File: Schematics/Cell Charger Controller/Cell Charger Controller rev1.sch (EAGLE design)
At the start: 17 parts, among them U1 HM2102NLT

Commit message: board almost done
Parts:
- added 12V_IN, CURRENT_IN, CURRENT_OUT: CONNECTOR-2, HyTechDevices:CONNECTOR-2
- added C2: 0.1uF, HyTechDevices:CAP0603-CAP
- added C3: 1uF, HyTechDevices:CAP0603-CAP
- added C6, C7: 10uF, HyTechDevices:CAP0603-CAP
- added D103: TS4148 RYG, HyTechDevices:DIODE0805
- added D104: MMBZ5246BLT1G, HyTechDevices:DIODE_ZENER
- added F1: 10A, HyTechDevices:FUSE_MINIBLADE
- added ISO-SPI, THERM1, THERM2, THERM3, THERM4, THERM5, THERM6, THERM7, THERM8, THERM9: CONNECTOR-2NANO-FIT_VERTICAL-2, HyTechDevices:CONNECTOR-2NANO-FIT_VERTICAL-2
- added Q1: DMG3406L, HyTechDevices:DMG3406LSOT
- added R14, R15, R16, R17, R18, R19, R20, R21, R22, R23: 10k, HyTechDevices:RESISTOR0603
- added U$10: OKI-78SR-5, HyTechDevices:OKI-78SR-5
- added U$4: INA260, HyTechDevices:INA260
- added U$5: MCP2562FD, HyTechDevices:MCP2562FD
- added U$6: ADAFRUIT_1824_KEYPAD, HyTechDevices:ADAFRUIT_1824_KEYPAD
- added U$7: ILI9341_TOUCH_SCREEN, HyTechDevices:ILI9341_TOUCH_SCREEN
- added U$8: G5LE-1A4, HyTechDevices:G5LE-1A4
- R10, R13, R9: value (none) -> 0
- R11, R12, R6, R7: value (none) -> 10k
- R8: value (none) -> 100
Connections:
- new net +12V: 12V_IN.1, C6.1, U$10.IN
- new net ALERT_INA: U$4.ALERT
- new net C1_KEYPAD: U$2.D35, U$6.C1
- new net C2_KEYPAD: U$2.D34, U$6.C2
- new net C3_KEYPAD: U$2.D33, U$6.C3
- new net CANH: U$5.7
- new net CANL: U$5.6
- new net CAN_RX: U$2.D0(RX1), U$5.4
- new net CAN_TX: U$2.D1(TX1), U$5.1
- new net CS_DISPLAY: U$2.D10, U$7.CS
- new net CS_DISPLAY_T: U$2.D9, U$7.T_CS
- new net CURRENT_IN: F1.2, U$8.P
- new net CURRENT_OUT: CURRENT_OUT.1, CURRENT_OUT.2, U$4.IN-
- new net D/C_DISPLAY: U$2.A1(RX3), U$7.DC
- new net IRQ_DISPLAY: U$2.D7(RX2), U$7.T_IRQ
- new net N$10: R8.1, U$7.LED
- new net N$11: CURRENT_IN.1, CURRENT_IN.2, F1.1
- new net N$12: R9.1, U$4.IN+, U$8.S
- new net N$15: D103.A, Q1.D, U$8.COIL+
- new net N$6: R11.2, R13.2, U$4.A1
- new net N$7: R10.1, R12.2, U$4.A0
- new net N$8: U$5.8
- new net N$9: R9.2, U$4.VBUS
- new net R1_KEYPAD: U$2.D32, U$6.R1
- new net R2_KEYPAD: U$2.D31(CANTX3), U$6.R2
- new net R3_KEYPAD: U$2.D30(CANRX3), U$6.R3
- new net R4_KEYPAD: U$2.D29, U$6.R4
- new net RELAY_CTRL: D104.C, Q1.G, R23.2, U$2.D5
- new net SCL_TEENSY: R7.2, U$2.A5, U$4.SCL
- new net SDA_TEENSY: R6.2, U$2.A4, U$4.SDA
- new net SENSE_THERM1: R14.1, THERM1.1, U$2.A14
- new net SENSE_THERM2: R15.1, THERM2.1, U$2.A15
- new net SENSE_THERM3: R16.1, THERM3.1, U$2.A16
- new net SENSE_THERM4: R17.1, THERM4.1, U$2.A17
- new net SENSE_THERM5: R18.1, THERM5.1, U$2.A2
- new net SENSE_THERM6: R19.1, THERM6.1, U$2.A10
- new net SENSE_THERM7: R20.1, THERM7.1, U$2.A11
- new net SENSE_THERM8: R21.1, THERM8.1, U$2.A12
- new net SENSE_THERM9: R22.1, THERM9.1, U$2.A13
- net +3V3: now also R8.2, U$2.3.3V, U$5.5, U$7.RESET
- net +5V: now also C2.1, C3.1, C7.1, D103.C, R10.2, R13.1, R14.2, R15.2, R16.2, R17.2, R18.2, R19.2, R20.2, R21.2, R22.2, R6.1, R7.1, U$10.OUT, U$4.VS, U$5.3, U$7.VCC, U$8.COIL-
- net CS_LTC6820: now also U$2.D6; no longer U$2.D10
- net GND: now also 12V_IN.2, C2.2, C3.2, C6.2, C7.2, D104.A, Q1.S, R11.1, R12.1, R23.1, THERM1.2, THERM2.2, THERM3.2, THERM4.2, THERM5.2, THERM6.2, THERM7.2, THERM8.2, THERM9.2, U$10.GND, U$2.GND, U$2.GND3, U$4.GND, U$5.2, U$7.GND
- net ISOSPI-N: now also ISO-SPI.2
- net ISOSPI-P: now also ISO-SPI.1
- net MISO_TEENSY: now also U$7.MISO, U$7.T_DO
- net MOSI_TEENSY: now also U$7.MOSI, U$7.T_DIN
- net SCK_TEENSY: now also U$7.SCK, U$7.T_CLK
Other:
- note added: "INA260"
- note added: "LTC6820"
- note added: "MCP2562"
- note added: "NOTE: Relay Coil Voltage - 5VDC"
- note added: "NOTE: The name of pins 5 and 8 on ths MCP2562 symbol are not correct, but the circuit should still work."
- moved on the sheet: C1, R1, R10, R11, R12, R13, R2, R3, R4, R5, R6, R7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

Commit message: charger controller board ready for review
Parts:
- added X1: CONNECTOR-4NANO-FIT-VERTICAL-4, HyTechDevices:CONNECTOR-4NANO-FIT-VERTICAL-4
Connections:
- net +12V: now also X1-1.S
- net ALERT_INA: now also U$2.A3
- net CANH: now also X1-4.S
- net CANL: now also X1-3.S
- net GND: now also X1-2.S
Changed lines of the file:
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@@
 <part name="D103" library="HyTechDevices" deviceset="DIODE" device="0805" value="TS4148 RYG"/>
 <part name="GND21" library="HyTechSupplies" deviceset="GND" device=""/>
+<part name="X1" library="HyTechDevices" deviceset="CONNECTOR-4" device="NANO-FIT-VERTICAL-4"/>
+<part name="GND22" library="HyTechSupplies" deviceset="GND" device=""/>
+<part name="P+14" library="HyTechSupplies" deviceset="+12V" device=""/>
 </parts>
 <sheets>
@@
 <attribute name="VALUE" x="215.9" y="208.28" size="1.778" layer="96"/>
 </instance>
+<instance part="X1" gate="-1" x="289.56" y="116.84" smashed="yes" rot="MR0">
+<attribute name="NAME" x="287.02" y="116.078" size="1.524" layer="95" rot="MR0"/>
+<attribute name="VALUE" x="295.402" y="120.777" size="1.778" layer="96" rot="MR0"/>
+</instance>
+<instance part="X1" gate="-2" x="289.56" y="114.3" smashed="yes" rot="MR0">
+<attribute name="NAME" x="287.02" y="113.538" size="1.524" layer="95" rot="MR0"/>
+</instance>
+<instance part="X1" gate="-3" x="289.56" y="111.76" smashed="yes" rot="MR0">
+<attribute name="NAME" x="287.02" y="110.998" size="1.524" layer="95" rot="MR0"/>
+</instance>
+<instance part="X1" gate="-4" x="289.56" y="109.22" smashed="yes" rot="MR0">
+<attribute name="NAME" x="287.02" y="108.458" size="1.524" layer="95" rot="MR0"/>
+</instance>
+<instance part="GND22" gate="1" x="302.26" y="111.76" smashed="yes" rot="MR0">
+<attribute name="VALUE" x="304.8" y="109.22" size="1.778" layer="96" rot="MR0"/>
+</instance>
+<instance part="P+14" gate="1" x="302.26" y="121.92" smashed="yes">
+<attribute name="VALUE" x="304.8" y="127" size="1.778" layer="96" rot="R180"/>
+</instance>
 </instances>
 <busses>
@@
 <pinref part="GND21" gate="1" pin="GND"/>
 <wire x1="218.44" y1="213.36" x2="218.44" y2="215.9" width="0.1524" layer="91"/>
+</segment>
+<segment>
+<pinref part="X1" gate="-2" pin="S"/>
+<wire x1="292.1" y1="114.3" x2="302.26" y2="114.3" width="0.1524" layer="91"/>
+<pinref part="GND22" gate="1" pin="GND"/>
 </segment>
 </net>
@@
 <label x="215.9" y="175.26" size="1.27" layer="95" rot="R180" xref="yes"/>
 </segment>
+<segment>
+<pinref part="U$2" gate="G$1" pin="A3"/>
+<wire x1="370.84" y1="187.96" x2="373.38" y2="187.96" width="0.1524" layer="91"/>
+<label x="373.38" y="187.96" size="1.27" layer="95" xref="yes"/>
+</segment>
 </net>
 <net name="N$6" class="0">
@@
 <pinref part="U$5" gate="G$1" pin="6"/>
 </segment>
+<segment>
+<pinref part="X1" gate="-3" pin="S"/>
+<wire x1="292.1" y1="111.76" x2="297.18" y2="111.76" width="0.1524" layer="91"/>
+<wire x1="297.18" y1="111.76" x2="297.18" y2="106.68" width="0.1524" layer="91"/>
+<wire x1="297.18" y1="106.68" x2="299.72" y2="106.68" width="0.1524" layer="91"/>
+<label x="299.72" y="106.68" size="1.27" layer="95" xref="yes"/>
+</segment>
 </net>
 <net name="CANH" class="0">
@@
 <label x="325.12" y="111.76" size="1.27" layer="95" rot="R180" xref="yes"/>
 <pinref part="U$5" gate="G$1" pin="7"/>
+</segment>
+<segment>
+<pinref part="X1" gate="-4" pin="S"/>
+<wire x1="292.1" y1="109.22" x2="294.64" y2="109.22" width="0.1524" layer="91"/>
+<wire x1="294.64" y1="109.22" x2="294.64" y2="104.14" width="0.1524" layer="91"/>
+<wire x1="294.64" y1="104.14" x2="299.72" y2="104.14" width="0.1524" layer="91"/>
+<label x="299.72" y="104.14" size="1.27" layer="95" xref="yes"/>
 </segment>
 </net>
@@
 <wire x1="345.44" y1="259.08" x2="345.44" y2="256.54" width="0.1524" layer="91"/>
 <junction x="345.44" y="256.54"/>
+</segment>
+<segment>
+<pinref part="X1" gate="-1" pin="S"/>
+<wire x1="292.1" y1="116.84" x2="302.26" y2="116.84" width="0.1524" layer="91"/>
+<wire x1="302.26" y1="116.84" x2="302.26" y2="119.38" width="0.1524" layer="91"/>
+<pinref part="P+14" gate="1" pin="+12V"/>
 </segment>
 </net>
@@
 </sheet>
 </sheets>
+<errors>
+</errors>
 </schematic>
 </drawing>

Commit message: small changes to the controller board
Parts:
- removed R9: 0, HyTechDevices:RESISTOR0603
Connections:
- removed net N$9: R9.2, U$4.VBUS
- net N$12: no longer R9.1
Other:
- note added: "Board power"
- note added: "Current sensing and main relay"
- note added: "Leonid Pozdneev"
- note added: "Microcontroller"
- note added: "Shematic for HyTech Racing battery cell charger controller board."
- note added: "Thermistor connections"
- note added: "User interface"
- note added: "isoSPI and CAN communications"
- moved on the sheet: 12V_IN, C1, C2, C3, C6, C7, ISO-SPI, R1, R14, R15, R16, R17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

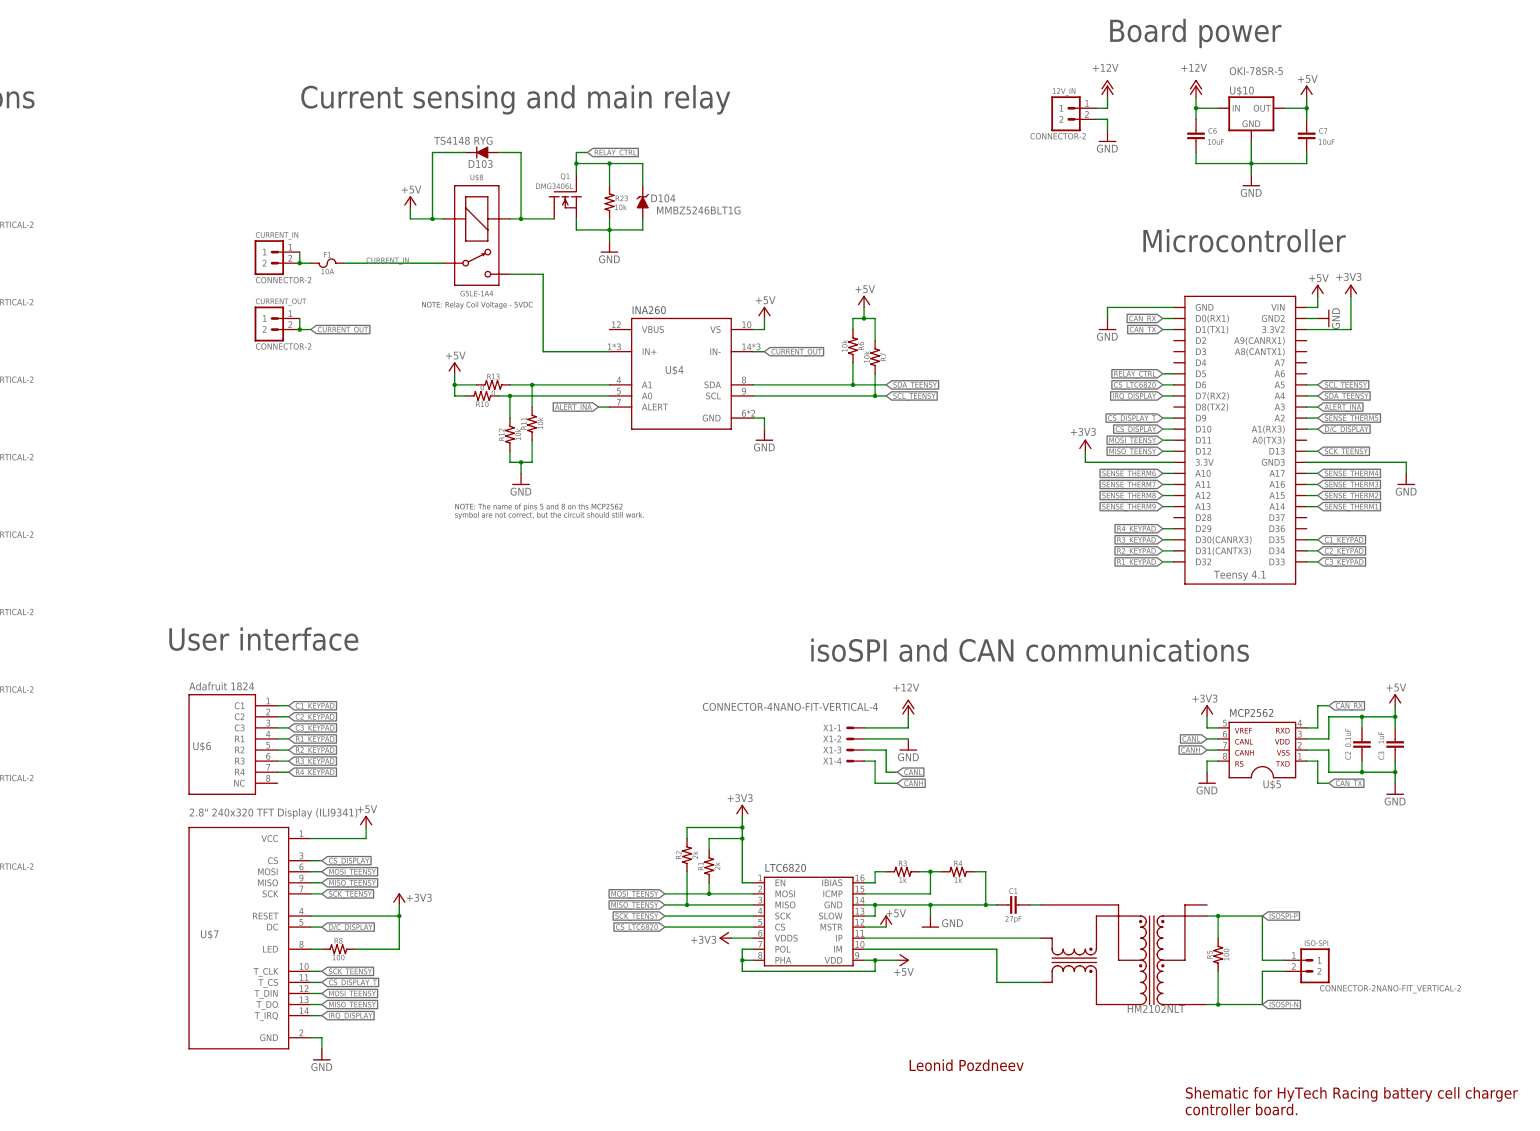
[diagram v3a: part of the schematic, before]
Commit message: generated gerbers for charger controller
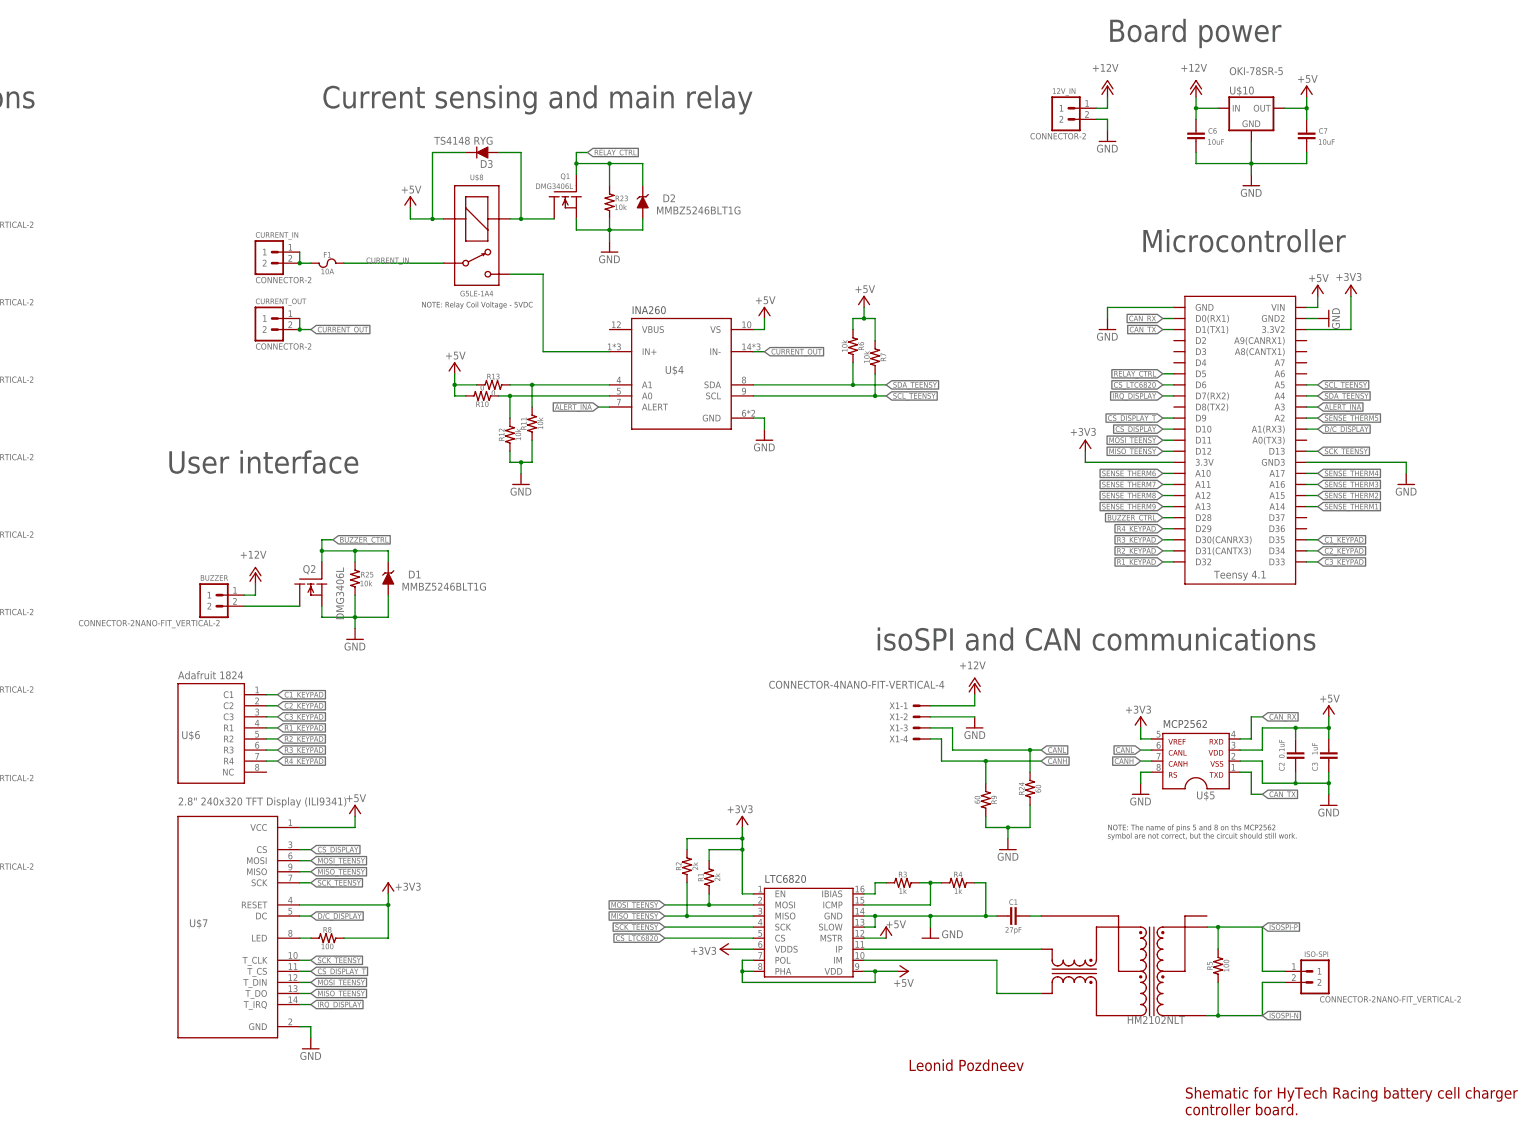
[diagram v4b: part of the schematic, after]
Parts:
- added BUZZER: CONNECTOR-2NANO-FIT_VERTICAL-2, HyTechDevices:CONNECTOR-2NANO-FIT_VERTICAL-2
- added D1: MMBZ5246BLT1G, HyTechDevices:DIODE_ZENER
- added Q2: DMG3406L, HyTechDevices:DMG3406LSOT
- added R24, R9: 60, HyTechDevices:RESISTOR0603
- added R25: 10k, HyTechDevices:RESISTOR0603
- renumbered D103 to D3, D104 to D2
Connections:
- removed net N$8: U$5.8
- new net BUZZER_CTRL: D1.C, Q2.G, R25.2, U$2.D28
- new net N$16: BUZZER.2, Q2.D
- net +12V: now also BUZZER.1
- net CANH: now also R9.1
- net CANL: now also R24.2
- net GND: now also D1.A, Q2.S, R24.1, R25.1, R9.2, U$5.8
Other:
- moved on the sheet: C1, C2, C3, ISO-SPI, R1, R2, R3, R4, R5, R8, U$5, U$6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
